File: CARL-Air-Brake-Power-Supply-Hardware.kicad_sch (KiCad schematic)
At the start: 85 parts, among them J1 Battery, J2 ICSP, J3 USB, J4 Raspberry Pi, J5 Servo, SW1 Power, U1 TPS56528, U2 TPS56528, U3 FT232RNL, U4 ATmega328P-AU, Y1 16MHz

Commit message: Assigned footprints
Assigned footprints to all symbols in circuit schematic.
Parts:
- C1, C10, C11, C12, C13, C14, C15, C16, C17, C18, C19, C2, C20, C21, C22, C23, C24, C25, C3, C4, C5, C6, C7, C8, C9: footprint (none) -> Local_Capacitor_SMD:Cap_Ceramic_0603
- D1, D2, D3: footprint (none) -> Local_Diode_SMD:Diode_DO-214AB_SMC
- D10, D6, D7, D8, D9: footprint (none) -> Local_LED_SMD:LED_Dual_Wuerth_WL-SBTW
- D11, D12, D13, D14, D4, D5: footprint (none) -> Local_LED_SMD:LED_0603
- F1: footprint (none) -> Local_Fuse_SMD:Fuse_PTC_1812
- J1: footprint (none) -> Local_Connector_ScrewTerminal:ScrewTerm_02_CUI_TB003-500-02BK
- J2: footprint (none) -> Local_Connector_PinHeader:PinHead_02x03_Pitch2.54mm_Bot3.00mm_Top6.00mm_Shroud2.50mm
- J3: footprint (none) -> Local_Connector_USB:USB_Micro_B_Recp_Wuerth_629105136821
- J4: footprint (none) -> Local_Connector_StackingHeader:StackHead_02x20_Pitch2.54mm_Bot10.50mm_Top8.50mm
- J5: footprint (none) -> Local_Connector_PinHeader:PinHead_02x02_Pitch2.54mm_Bot3.00mm_Top6.00mm_Shroud2.50mm
- L1, L2: footprint (none) -> Local_Inductor_SMD:Ind_Eaton_DR127
- R1, R10, R11, R12, R13, R14, R15, R16, R17, R18, R19, R2, R20, R21, R22, R23, R24, R25, R26, R27, R3, R4, R5, R6, R7, R8, R9: footprint (none) -> Local_Resistor_SMD:Res_Film_0603
- SW1: footprint (none) -> Local_Switch_THT:Switch_SPDT_Salecom_T80-S-TS-13P-A1-2-R
- TP1, TP2, TP3, TP4, TP5: footprint (none) -> Local_TestPoint:TestPoint_CircPad2.00mm_CircMsk2.50mm
- U1, U2: footprint (none) -> Local_Package_SOIC:SOIC_08_Dim4.00x5.00x1.70mm_Pitch1.27mm_RectThPad2.95x4.90mm_RectMsk2.40x3.10mm
- U3: footprint (none) -> Local_Package_SOIC:SOIC_28_Dim5.50x10.50x2.00mm_Pitch0.65mm
- U4: footprint (none) -> Local_Package_QFP:TQFP_08x08_Dim7.00x7.00x1.20mm_Pitch0.80mm
- Y1: footprint (none) -> Local_Crystal_SMD:Crystal_HC49-US

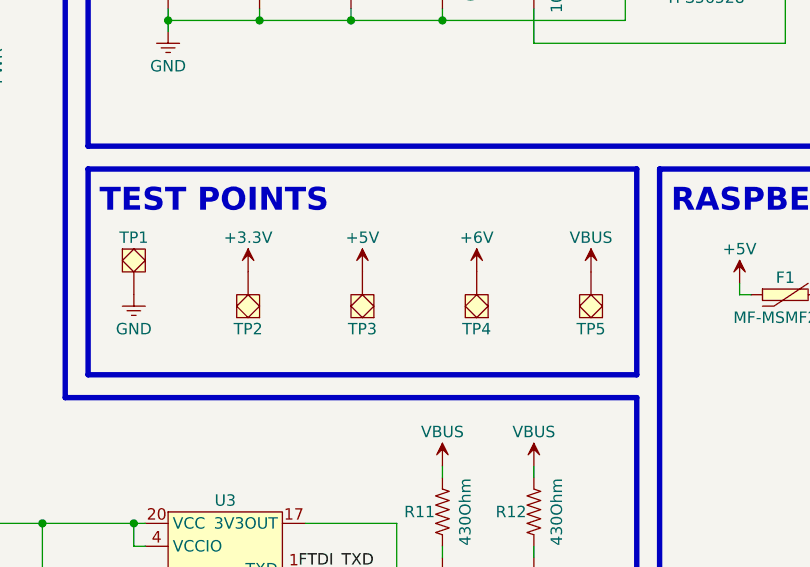
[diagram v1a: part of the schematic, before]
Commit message: Added test point for VBAT
Added test point for VBAT line and updated PCB accordingly.
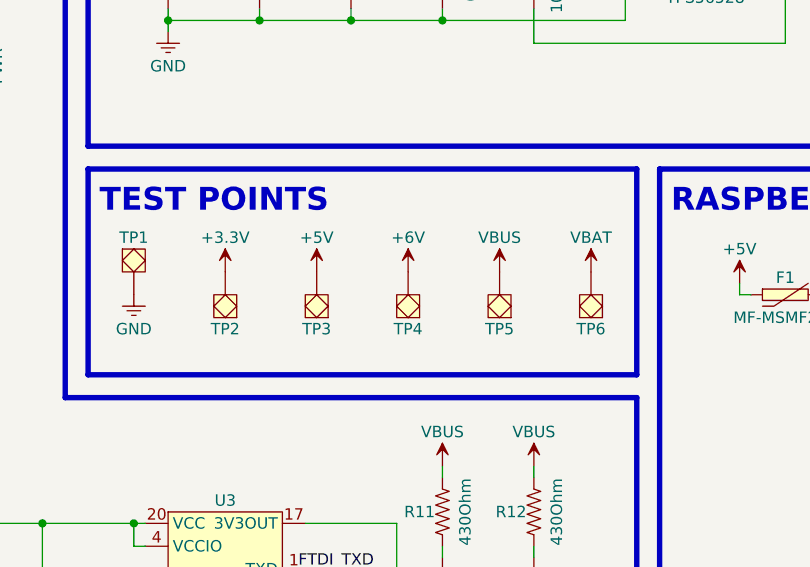
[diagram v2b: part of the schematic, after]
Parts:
- added TP6: ~, Local_TestPoint:TestPoint_CircPad2.00mm_CircMsk2.50mm, symbol Local_TestPoint:TestPoint
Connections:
- net VBAT: now also TP6.1
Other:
- moved on the sheet: TP2, TP3, TP4, TP5
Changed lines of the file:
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@@
     )
   )
-  (symbol (lib_id "Local_Power:+3.3V") (at 69.85 114.3 0) (unit 1)
+  (symbol (lib_id "Local_Power:+3.3V") (at 67.31 114.3 0) (unit 1)
     (in_bom no) (on_board no) (dnp no)
-    (property "Reference" "#PWR039" (at 69.85 114.3 0)
+    (property "Reference" "#PWR039" (at 67.31 114.3 0)
       (effects (font (size 1.27 1.27)) hide)
     )
-    (property "Value" "+3.3V" (at 69.85 110.49 0)
+    (property "Value" "+3.3V" (at 67.31 110.49 0)
       (effects (font (size 1.27 1.27)))
     )
-    (property "Footprint" "" (at 69.85 114.3 0)
+    (property "Footprint" "" (at 67.31 114.3 0)
       (effects (font (size 1.27 1.27)) hide)
     )
-    (property "Datasheet" "" (at 69.85 114.3 0)
+    (property "Datasheet" "" (at 67.31 114.3 0)
       (effects (font (size 1.27 1.27)) hide)
     )
@@
     )
   )
-  (symbol (lib_id "Local_TestPoint:TestPoint") (at 95.25 114.3 180) (unit 1)
+  (symbol (lib_id "Local_TestPoint:TestPoint") (at 87.63 114.3 180) (unit 1)
     (in_bom yes) (on_board yes) (dnp no)
-    (property "Reference" "TP4" (at 95.25 120.65 0)
+    (property "Reference" "TP4" (at 87.63 120.65 0)
       (effects (font (size 1.27 1.27)))
     )
-    (property "Value" "~" (at 95.25 118.11 0)
+    (property "Value" "~" (at 87.63 118.11 0)
       (effects (font (size 1.27 1.27)))
     )
-    (property "Footprint" "Local_TestPoint:TestPoint_CircPad2.00mm_CircMsk2.50mm" (at 95.25 114.3 0)
+    (property "Footprint" "Local_TestPoint:TestPoint_CircPad2.00mm_CircMsk2.50mm" (at 87.63 114.3 0)
       (effects (font (size 1.27 1.27)) hide)
     )
-    (property "Datasheet" "" (at 95.25 114.3 0)
+    (property "Datasheet" "" (at 87.63 114.3 0)
       (effects (font (size 1.27 1.27)) hide)
     )
@@
     )
   )
-  (symbol (lib_id "Local_Power:+5V") (at 82.55 114.3 0) (unit 1)
+  (symbol (lib_id "Local_Power:+5V") (at 77.47 114.3 0) (unit 1)
     (in_bom no) (on_board no) (dnp no)
-    (property "Reference" "#PWR040" (at 82.55 114.3 0)
+    (property "Reference" "#PWR040" (at 77.47 114.3 0)
       (effects (font (size 1.27 1.27)) hide)
     )
-    (property "Value" "+5V" (at 82.55 110.49 0)
+    (property "Value" "+5V" (at 77.47 110.49 0)
       (effects (font (size 1.27 1.27)))
     )
-    (property "Footprint" "" (at 82.55 114.3 0)
+    (property "Footprint" "" (at 77.47 114.3 0)
       (effects (font (size 1.27 1.27)) hide)
     )
-    (property "Datasheet" "" (at 82.55 114.3 0)
+    (property "Datasheet" "" (at 77.47 114.3 0)
       (effects (font (size 1.27 1.27)) hide)
     )
@@
     )
   )
+  (symbol (lib_id "Local_TestPoint:TestPoint") (at 107.95 114.3 180) (unit 1)
+    (in_bom yes) (on_board yes) (dnp no)
+    (property "Reference" "TP6" (at 107.95 120.65 0)
+      (effects (font (size 1.27 1.27)))
+    )
+    (property "Value" "~" (at 107.95 118.11 0)
+      (effects (font (size 1.27 1.27)))
+    )
+    (property "Footprint" "Local_TestPoint:TestPoint_CircPad2.00mm_CircMsk2.50mm" (at 107.95 114.3 0)
+      (effects (font (size 1.27 1.27)) hide)
+    )
+    (property "Datasheet" "" (at 107.95 114.3 0)
+      (effects (font (size 1.27 1.27)) hide)
+    )
+    (pin "1")
+    (instances
+      (project "CARL-Air-Brake-Power-Supply-Hardware"
+        (path "/a14588cc-c6b5-4cd2-a60d-abff4b7f3fc4"
+          (reference "TP6") (unit 1)
+        )
+      )
+    )
+  )
   (symbol (lib_id "Local_PowerMgmt_TI:TPS56528") (at 120.65 38.1 0) (unit 1)
     (in_bom yes) (on_board yes) (dnp no)
@@
     )
   )
+  (symbol (lib_id "Local_Power:VBAT") (at 107.95 114.3 0) (unit 1)
+    (in_bom no) (on_board no) (dnp no)
+    (property "Reference" "#PWR056" (at 107.95 114.3 0)
+      (effects (font (size 1.27 1.27)) hide)
+    )
+    (property "Value" "VBAT" (at 107.95 110.49 0)
+      (effects (font (size 1.27 1.27)))
+    )
+    (property "Footprint" "" (at 107.95 114.3 0)
+      (effects (font (size 1.27 1.27)) hide)
+    )
+    (property "Datasheet" "" (at 107.95 114.3 0)
+      (effects (font (size 1.27 1.27)) hide)
+    )
+    (pin "1")
+    (instances
+      (project "CARL-Air-Brake-Power-Supply-Hardware"
+        (path "/a14588cc-c6b5-4cd2-a60d-abff4b7f3fc4"
+          (reference "#PWR056") (unit 1)
+        )
+      )
+    )
+  )
   (symbol (lib_id "Local_Resistor:Res") (at 204.47 111.76 0) (unit 1)
     (in_bom yes) (on_board yes) (dnp no)
@@
     )
   )
-  (symbol (lib_id "Local_Power:VBUS") (at 107.95 114.3 0) (unit 1)
+  (symbol (lib_id "Local_Power:VBUS") (at 97.79 114.3 0) (unit 1)
     (in_bom no) (on_board no) (dnp no)
-    (property "Reference" "#PWR042" (at 107.95 114.3 0)
+    (property "Reference" "#PWR042" (at 97.79 114.3 0)
       (effects (font (size 1.27 1.27)) hide)
     )
-    (property "Value" "VBUS" (at 107.95 110.49 0)
+    (property "Value" "VBUS" (at 97.79 110.49 0)
       (effects (font (size 1.27 1.27)))
     )
-    (property "Footprint" "" (at 107.95 114.3 0)
+    (property "Footprint" "" (at 97.79 114.3 0)
       (effects (font (size 1.27 1.27)) hide)
     )
-    (property "Datasheet" "" (at 107.95 114.3 0)
+    (property "Datasheet" "" (at 97.79 114.3 0)
       (effects (font (size 1.27 1.27)) hide)
     )
@@
     )
   )
-  (symbol (lib_id "Local_Power:+6V") (at 95.25 114.3 0) (unit 1)
+  (symbol (lib_id "Local_Power:+6V") (at 87.63 114.3 0) (unit 1)
     (in_bom no) (on_board no) (dnp no)
-    (property "Reference" "#PWR041" (at 95.25 114.3 0)
+    (property "Reference" "#PWR041" (at 87.63 114.3 0)
       (effects (font (size 1.27 1.27)) hide)
     )
-    (property "Value" "+6V" (at 95.25 110.49 0)
+    (property "Value" "+6V" (at 87.63 110.49 0)
       (effects (font (size 1.27 1.27)))
     )
-    (property "Footprint" "" (at 95.25 114.3 0)
+    (property "Footprint" "" (at 87.63 114.3 0)
       (effects (font (size 1.27 1.27)) hide)
     )
-    (property "Datasheet" "" (at 95.25 114.3 0)
+    (property "Datasheet" "" (at 87.63 114.3 0)
       (effects (font (size 1.27 1.27)) hide)
     )
@@
     )
   )
-  (symbol (lib_id "Local_TestPoint:TestPoint") (at 82.55 114.3 180) (unit 1)
+  (symbol (lib_id "Local_TestPoint:TestPoint") (at 77.47 114.3 180) (unit 1)
     (in_bom yes) (on_board yes) (dnp no)
-    (property "Reference" "TP3" (at 82.55 120.65 0)
+    (property "Reference" "TP3" (at 77.47 120.65 0)
       (effects (font (size 1.27 1.27)))
     )
-    (property "Value" "~" (at 82.55 118.11 0)
+    (property "Value" "~" (at 77.47 118.11 0)
       (effects (font (size 1.27 1.27)))
     )
-    (property "Footprint" "Local_TestPoint:TestPoint_CircPad2.00mm_CircMsk2.50mm" (at 82.55 114.3 0)
+    (property "Footprint" "Local_TestPoint:TestPoint_CircPad2.00mm_CircMsk2.50mm" (at 77.47 114.3 0)
       (effects (font (size 1.27 1.27)) hide)
     )
-    (property "Datasheet" "" (at 82.55 114.3 0)
+    (property "Datasheet" "" (at 77.47 114.3 0)
       (effects (font (size 1.27 1.27)) hide)
     )
@@
     )
   )
-  (symbol (lib_id "Local_TestPoint:TestPoint") (at 69.85 114.3 180) (unit 1)
+  (symbol (lib_id "Local_TestPoint:TestPoint") (at 67.31 114.3 180) (unit 1)
     (in_bom yes) (on_board yes) (dnp no)
-    (property "Reference" "TP2" (at 69.85 120.65 0)
+    (property "Reference" "TP2" (at 67.31 120.65 0)
       (effects (font (size 1.27 1.27)))
     )
-    (property "Value" "~" (at 69.85 118.11 0)
+    (property "Value" "~" (at 67.31 118.11 0)
       (effects (font (size 1.27 1.27)))
     )
-    (property "Footprint" "Local_TestPoint:TestPoint_CircPad2.00mm_CircMsk2.50mm" (at 69.85 114.3 0)
+    (property "Footprint" "Local_TestPoint:TestPoint_CircPad2.00mm_CircMsk2.50mm" (at 67.31 114.3 0)
       (effects (font (size 1.27 1.27)) hide)
     )
-    (property "Datasheet" "" (at 69.85 114.3 0)
+    (property "Datasheet" "" (at 67.31 114.3 0)
       (effects (font (size 1.27 1.27)) hide)
     )
@@
     )
   )
-  (symbol (lib_id "Local_TestPoint:TestPoint") (at 107.95 114.3 180) (unit 1)
+  (symbol (lib_id "Local_TestPoint:TestPoint") (at 97.79 114.3 180) (unit 1)
     (in_bom yes) (on_board yes) (dnp no)
-    (property "Reference" "TP5" (at 107.95 120.65 0)
+    (property "Reference" "TP5" (at 97.79 120.65 0)
       (effects (font (size 1.27 1.27)))
     )
-    (property "Value" "~" (at 107.95 118.11 0)
+    (property "Value" "~" (at 97.79 118.11 0)
       (effects (font (size 1.27 1.27)))
     )
-    (property "Footprint" "Local_TestPoint:TestPoint_CircPad2.00mm_CircMsk2.50mm" (at 107.95 114.3 0)
+    (property "Footprint" "Local_TestPoint:TestPoint_CircPad2.00mm_CircMsk2.50mm" (at 97.79 114.3 0)
       (effects (font (size 1.27 1.27)) hide)
     )
-    (property "Datasheet" "" (at 107.95 114.3 0)
+    (property "Datasheet" "" (at 97.79 114.3 0)
       (effects (font (size 1.27 1.27)) hide)
     )

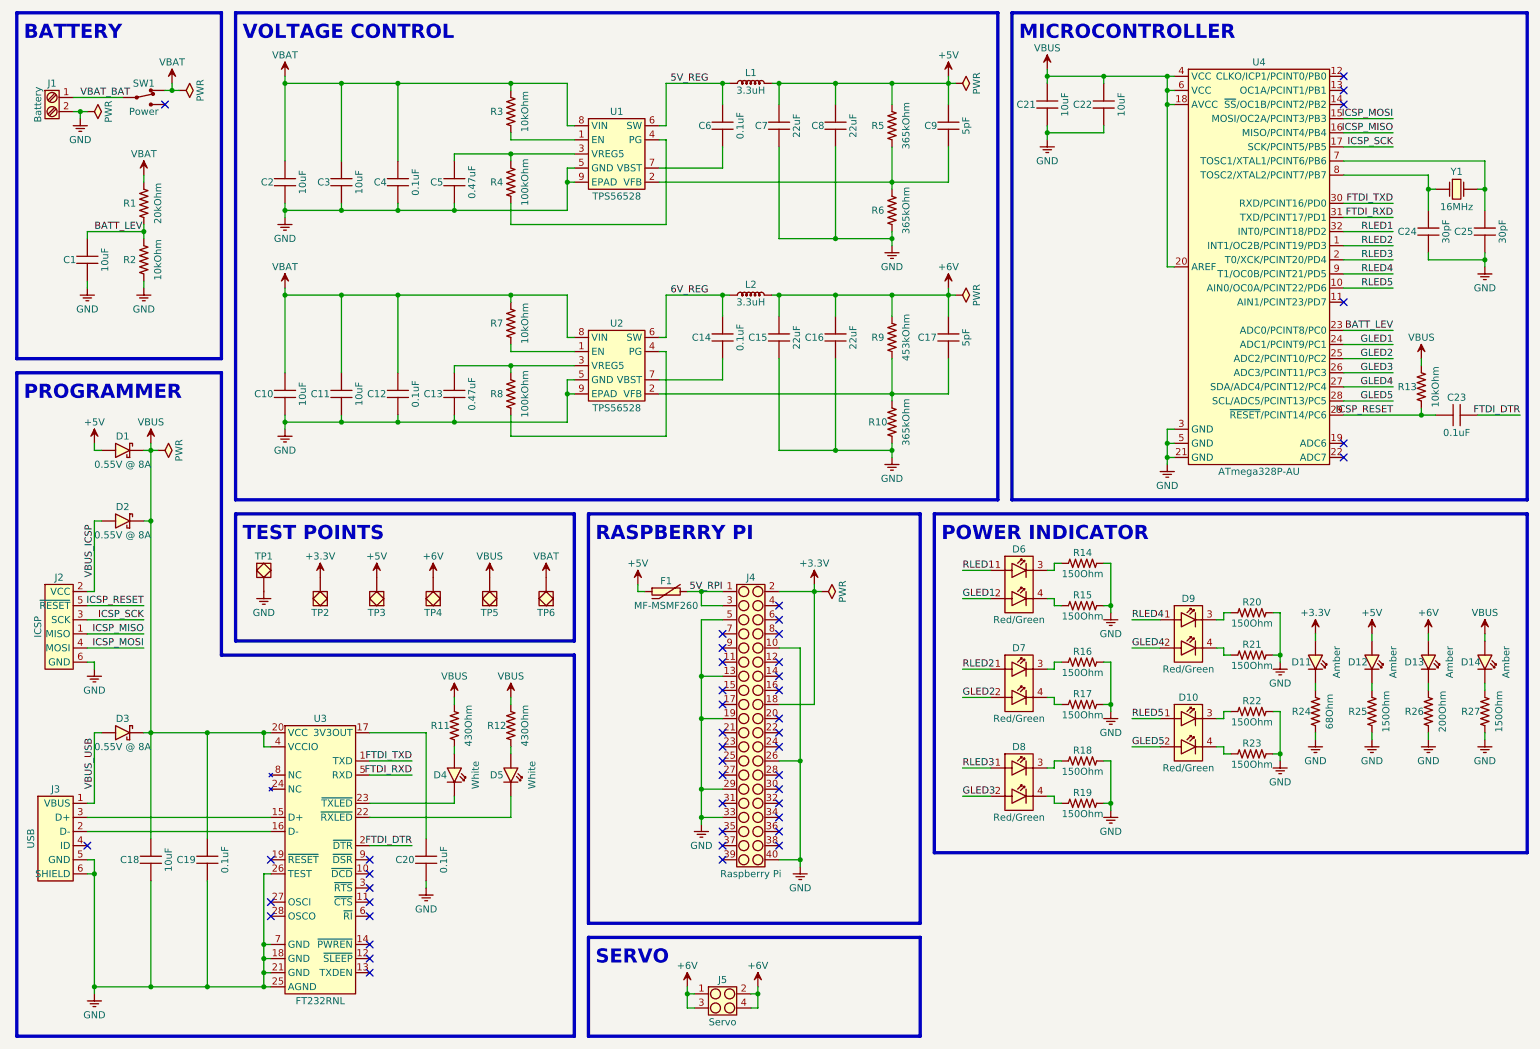
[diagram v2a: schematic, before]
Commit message: Changed VBUS to VMCU
Changed name of VBUS net to VMCU in schematic and board files.
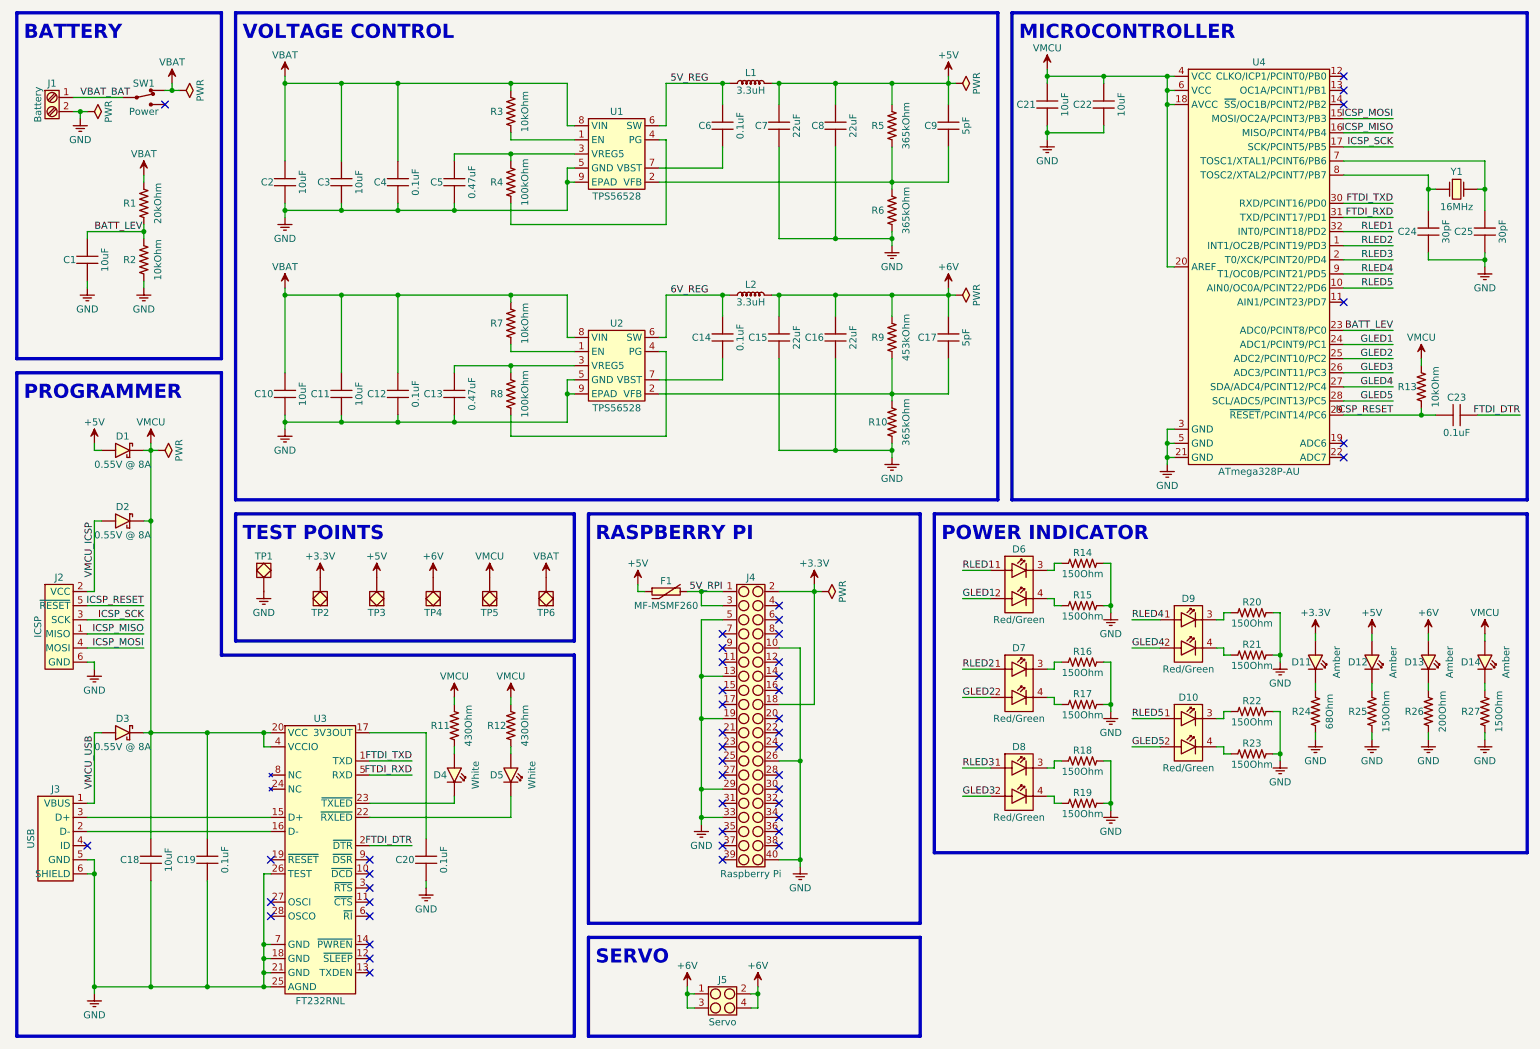
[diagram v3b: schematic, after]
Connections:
- net VBUS renamed VMCU
- net VBUS_ICSP renamed VMCU_ICSP
- net VBUS_USB renamed VMCU_USB

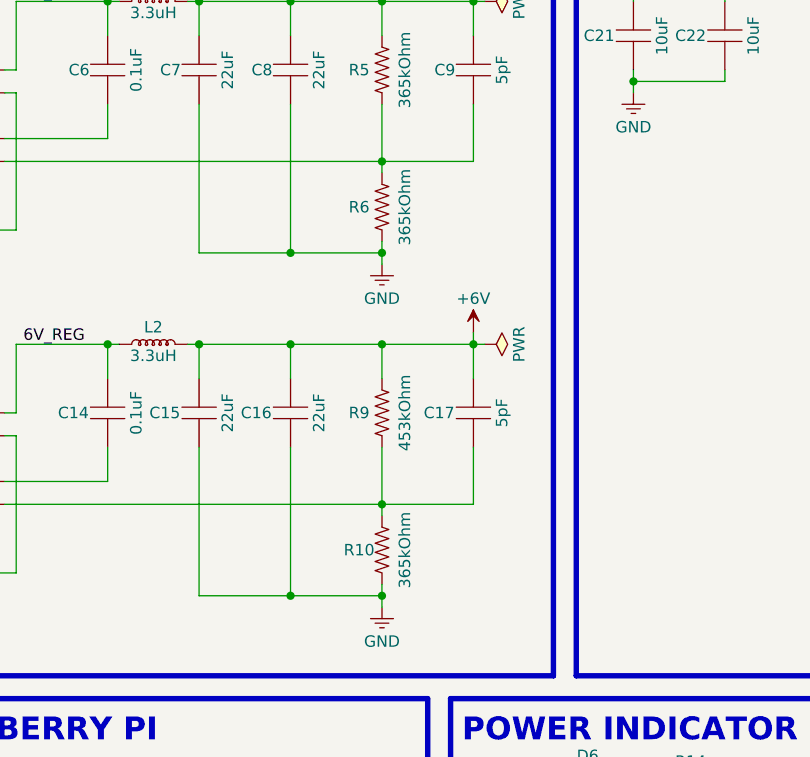
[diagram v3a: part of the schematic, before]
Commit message: Corrected component values
Corrected resistance values of resistors R6 and R10.
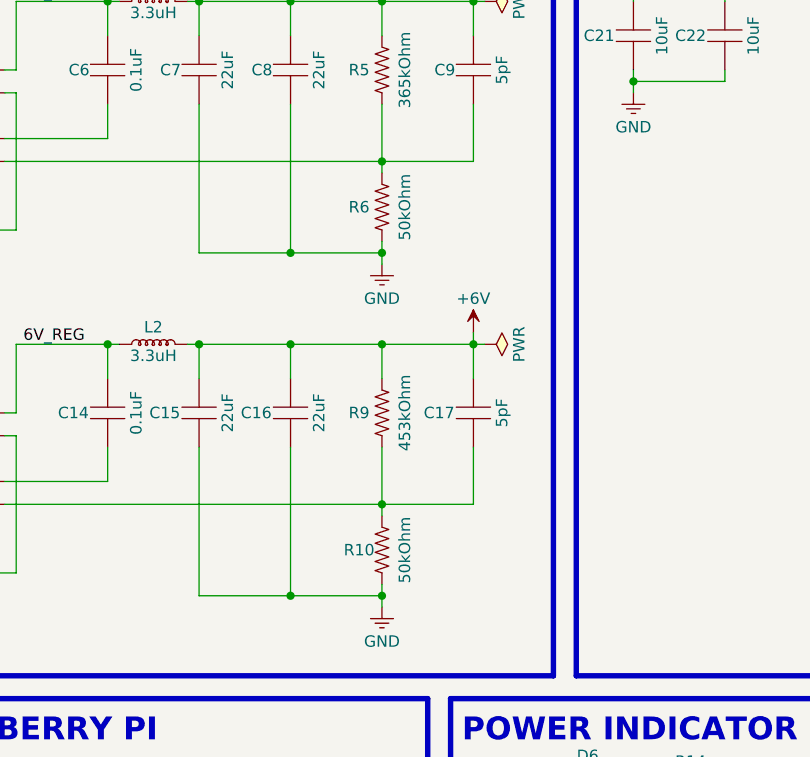
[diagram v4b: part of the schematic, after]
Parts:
- R10, R6: value 365kOhm -> 50kOhm
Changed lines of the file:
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@@
       (effects (font (size 1.27 1.27)))
     )
-    (property "Value" "365kOhm" (at 172.72 48.26 0)
+    (property "Value" "50kOhm" (at 172.72 48.26 0)
       (effects (font (size 1.27 1.27)))
     )
@@
       (effects (font (size 1.27 1.27)))
     )
-    (property "Value" "365kOhm" (at 172.72 86.36 0)
-      (effects (font (size 1.27 1.27)))
-    )
+    (property "Value" "50kOhm" (at 172.72 86.36 0)
+      (effects (font (size 1.27 1.27)))
+    )
